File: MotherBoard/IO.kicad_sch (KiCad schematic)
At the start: 9 parts, among them J301 1376357-3, J302 Conn_01x04_Pin, J303 430450200

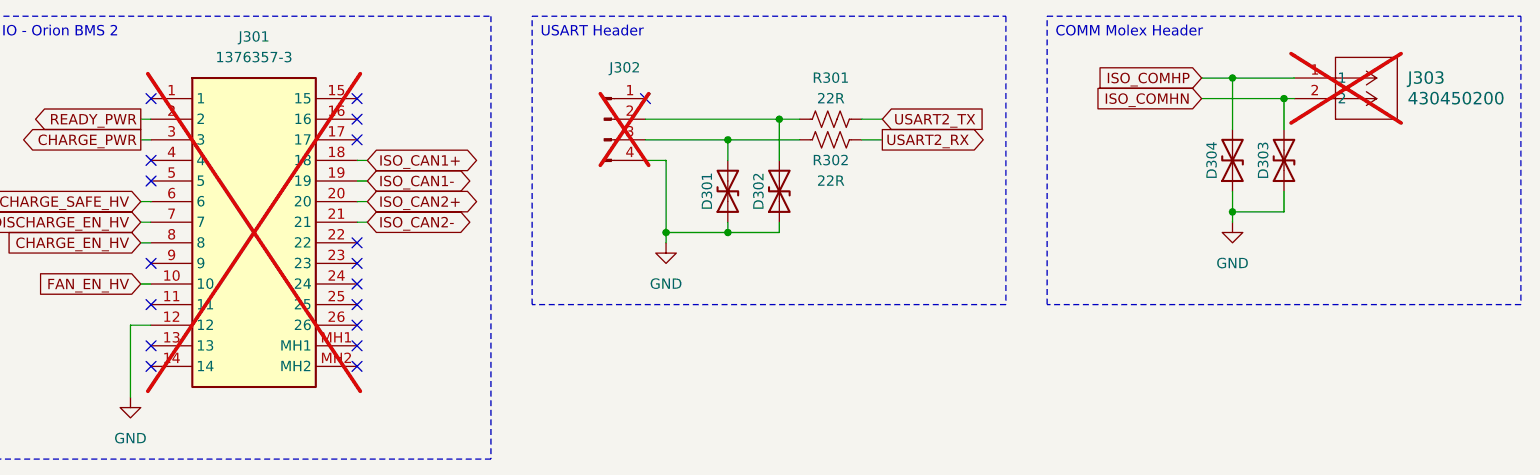
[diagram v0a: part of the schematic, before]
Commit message: BOM completed + All 3D models added + Initial board shape complete
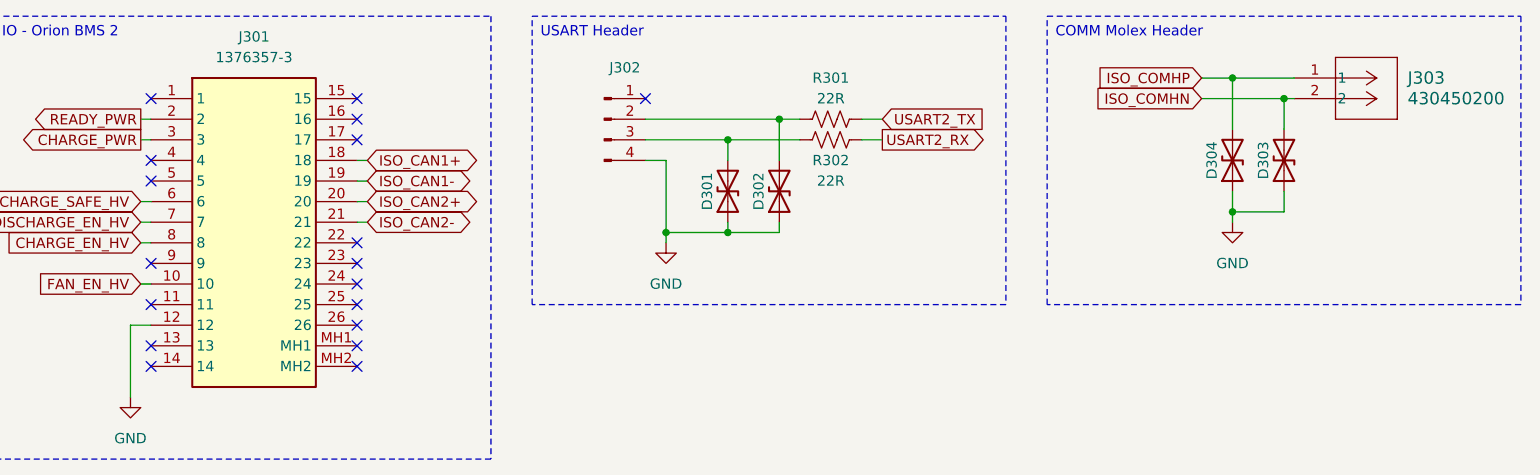
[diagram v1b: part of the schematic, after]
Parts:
- J301, J302, J303: now fitted
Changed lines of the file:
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@@
 		(in_bom yes)
 		(on_board yes)
-		(dnp yes)
+		(dnp no)
 		(property "Reference" "J302"
 			(at 106.68 31.75 0)
@@
 		(in_bom yes)
 		(on_board yes)
-		(dnp yes)
+		(dnp no)
 		(fields_autoplaced yes)
 		(property "Reference" "J301"
@@
 		(in_bom yes)
 		(on_board yes)
-		(dnp yes)
+		(dnp no)
 		(fields_autoplaced yes)
 		(property "Reference" "J303"

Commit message: Finished layout need to route
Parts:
- added D? (x2): D_TVS, Diode_SMD:D_SOD-323, symbol Device:D_TVS
- added J?: 430450200, molex_comm:CON_430450200_MOL, symbol molex_comm:430450200
- renumbered D304 to D303, D303 to D304
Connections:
- net GND: now also D?.1 (A1), D?.1 (A1)
- new net ISO_COMLN: D?.2 (A2), J?.2
- new net ISO_COMLP: D?.2 (A2), J?.1

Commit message: Finished motherboard. Need to review BOM
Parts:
- removed D304, D? (x2): D_TVS, Diode_SMD:D_SOD-323, symbol Device:D_TVS
- added C301: 1u, Capacitor_SMD:C_0402_1005Metric, symbol Device:C
- added D301, D305: D_TVS, Diode_SMD:D_SOD-323, symbol Device:D_TVS
- added F301, F302: Fuse, Fuse:Fuse_0805_2012Metric, symbol Device:Fuse
- added J301: Conn_01x04_Pin, Connector_PinHeader_2.54mm:PinHeader_1x04_P2.54mm_Vertical, symbol Connector:Conn_01x04_Pin
- added J306: Conn_01x02_Pin, Connector_PinHeader_2.54mm:PinHeader_1x02_P2.54mm_Vertical, symbol Connector:Conn_01x02_Pin
- added R301, R302: 22R, Resistor_SMD:R_1206_3216Metric, symbol Device:R_US
- added R305: 2.2k, Resistor_SMD:R_1206_3216Metric, symbol Device:R_US
- D303: Manufacturer_Part_Number (none) -> PESD3V3L1BA,115
- gave numbers to parts that had none: 1
- renumbered D301 to D302, D302 to D304, J301 to J303, J303 to J304, R301 to R303, R302 to R304
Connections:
- net GND: now also J302.1 (Pin_1), C301.2, D301.1 (A1), D305.1 (A1), J301.1 (Pin_1), J306.1 (Pin_1); no longer J302.4 (Pin_4)
- net ISO_COMHP: no longer D303.2 (A2)
- new net: D301.2 (A2), J301.3 (Pin_3), R302.1
- new net: D303.2 (A2), J301.2 (Pin_2), R301.1
- new net: F301.2, J301.4 (Pin_4)
- new net: D305.2 (A2), J306.2 (Pin_2), R305.1
- new net: F302.2, J302.4 (Pin_4)
- new net +5V: F301.1, F302.1
- new net ADC_IN: C301.1, R305.2
- new net UART4_RX: R302.2
- new net UART4_TX: R301.2
- no-connect marks 18 -> 17
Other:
- moved on the sheet: D302, D304, J302, J303, J304, J305, R303, R304

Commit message: Fixed power routing mistake + finished BOM + generated manufacturing files
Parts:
- D305: Manufacturer_Part_Number (none) -> PESD3V3L1BA,115
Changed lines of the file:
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@@
+			)
+		)
+		(property "JLC" ""
+			(at 59.69 167.64 0)
+			(effects
+				(font
+					(size 1.27 1.27)
+				)
+				(hide yes)
 			)
 		)
@@
 			)
 		)
+		(property "JLC" ""
+			(at 59.69 165.1 0)
+			(effects
+				(font
+					(size 1.27 1.27)
+				)
+				(hide yes)
+			)
+		)
 		(pin "2"
 		)
@@
 		)
 		(property "Sim.Type" ""
+			(at 31.75 165.1 0)
+			(effects
+				(font
+					(size 1.27 1.27)
+				)
+				(hide yes)
+			)
+		)
+		(property "JLC" ""
 			(at 31.75 165.1 0)
 			(effects
@@
 			)
 		)
+		(property "JLC" ""
+			(at 160.02 36.83 0)
+			(effects
+				(font
+					(size 1.27 1.27)
+				)
+				(hide yes)
+			)
+		)
 		(pin "1"
 		)
@@
 			)
 		)
+		(property "Manufacturer_Part_Number" "PESD3V3L1BA,115"
+			(at 175.26 41.91 0)
+			(effects
+				(font
+					(size 1.27 1.27)
+				)
+				(hide yes)
+			)
+		)
+		(property "JLC" ""
+			(at 175.26 41.91 0)
+			(effects
+				(font
+					(size 1.27 1.27)
+				)
+				(hide yes)
+			)
+		)
 		(pin "1"
 		)
@@
 		)
 		(property "Sim.Type" ""
+			(at 33.02 121.92 0)
+			(effects
+				(font
+					(size 1.27 1.27)
+				)
+				(hide yes)
+			)
+		)
+		(property "JLC" ""
 			(at 33.02 121.92 0)
 			(effects
@@
 			)
 		)
+		(property "JLC" ""
+			(at 60.96 124.46 0)
+			(effects
+				(font
+					(size 1.27 1.27)
+				)
+				(hide yes)
+			)
+		)
 		(pin "2"
 		)
@@
 			)
 		)
+		(property "JLC" ""
+			(at 53.34 173.99 0)
+			(effects
+				(font
+					(size 1.27 1.27)
+				)
+				(hide yes)
+			)
+		)
 		(pin "1"
 		)
@@
 		)
 		(property "Manufacturer_Part_Number" "PESD3V3L1BA,115"
+			(at 54.61 130.81 0)
+			(effects
+				(font
+					(size 1.27 1.27)
+				)
+				(hide yes)
+			)
+		)
+		(property "JLC" ""
 			(at 54.61 130.81 0)
 			(effects
@@
 			)
 		)
+		(property "JLC" ""
+			(at 43.18 160.02 0)
+			(effects
+				(font
+					(size 1.27 1.27)
+				)
+				(hide yes)
+			)
+		)
 		(pin "1"
 		)
@@
 		)
 		(property "Manufacturer_Part_Number" "FRC1206J220 TS"
+			(at 181.61 36.83 0)
+			(effects
+				(font
+					(size 1.27 1.27)
+				)
+				(hide yes)
+			)
+		)
+		(property "JLC" ""
 			(at 181.61 36.83 0)
 			(effects
@@
 			)
 		)
+		(property "JLC" ""
+			(at 46.99 43.18 0)
+			(effects
+				(font
+					(size 1.27 1.27)
+				)
+				(hide yes)
+			)
+		)
 		(pin "14"
 		)
@@
 			)
 		)
+		(property "JLC" ""
+			(at 123.19 33.02 0)
+			(effects
+				(font
+					(size 1.27 1.27)
+				)
+				(hide yes)
+			)
+		)
 		(pin "1"
 		)
@@
 		)
 		(property "Manufacturer_Part_Number" "PESD3V3L1BA,115"
+			(at 46.99 173.99 0)
+			(effects
+				(font
+					(size 1.27 1.27)
+				)
+				(hide yes)
+			)
+		)
+		(property "JLC" ""
 			(at 46.99 173.99 0)
 			(effects
@@
 			)
 		)
+		(property "JLC" ""
+			(at 44.45 115.57 0)
+			(effects
+				(font
+					(size 1.27 1.27)
+				)
+				(hide yes)
+			)
+		)
 		(pin "1"
 		)
@@
 			)
 		)
+		(property "JLC" ""
+			(at 123.19 81.28 0)
+			(effects
+				(font
+					(size 1.27 1.27)
+				)
+				(hide yes)
+			)
+		)
 		(pin "1"
 		)
@@
 			)
 		)
+		(property "JLC" ""
+			(at 190.5 41.91 0)
+			(effects
+				(font
+					(size 1.27 1.27)
+				)
+				(hide yes)
+			)
+		)
 		(pin "1"
 		)
@@
 			)
 		)
+		(property "JLC" ""
+			(at 48.26 130.81 0)
+			(effects
+				(font
+					(size 1.27 1.27)
+				)
+				(hide yes)
+			)
+		)
 		(pin "1"
 		)
@@
 			(at 60.96 121.92 0)
 			(effects
+				(font
+					(size 1.27 1.27)
+				)
+				(hide yes)
+			)
+		)
+		(property "JLC" ""
+			(at 60.96 121.92 0)
+			(effects

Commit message: Daughterboard 100% Complete + Edited Motherboard BOM
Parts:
- J301, J302, J303, J304, J305, J306: now not fitted
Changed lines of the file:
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@@
 		(in_bom yes)
 		(on_board yes)
-		(dnp no)
+		(dnp yes)
 		(property "Reference" "J301"
 			(at 34.29 158.75 0)
@@
 		(in_bom yes)
 		(on_board yes)
-		(dnp no)
+		(dnp yes)
 		(fields_autoplaced yes)
 		(property "Reference" "J306"
@@
 		(in_bom yes)
 		(on_board yes)
-		(dnp no)
+		(dnp yes)
 		(property "Reference" "J302"
 			(at 35.56 115.57 0)
@@
 		(in_bom yes)
 		(on_board yes)
-		(dnp no)
+		(dnp yes)
 		(fields_autoplaced yes)
 		(property "Reference" "J303"
@@
 		(in_bom yes)
 		(on_board yes)
-		(dnp no)
+		(dnp yes)
 		(fields_autoplaced yes)
 		(property "Reference" "J304"
@@
 		(in_bom yes)
 		(on_board yes)
-		(dnp no)
+		(dnp yes)
 		(fields_autoplaced yes)
 		(property "Reference" "J305"

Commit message: Both boards complete
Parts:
- C301: JLCPCB Part # (none) -> C29266
- D301, D302, D303, D304, D305: JLCPCB Part # (none) -> C51450
- F301, F302: JLCPCB Part # (none) -> C269104
- R301, R302, R303, R304: JLCPCB Part # (none) -> C2907457
- R305: JLCPCB Part # (none) -> C26038; Manufacturer_Part_Number FRC1206J220 TS -> 1206W4J0222T5E
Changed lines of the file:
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@@
 			)
 		)
-		(property "JLC" ""
+		(property "JLCPCB Part #" "C2907457"
 			(at 59.69 167.64 0)
 			(effects
@@
 			)
 		)
-		(property "JLC" ""
+		(property "JLCPCB Part #" "C2907457"
 			(at 59.69 165.1 0)
 			(effects
@@
 		)
 		(property "Sim.Type" ""
-			(at 31.75 165.1 0)
-			(effects
-				(font
-					(size 1.27 1.27)
-				)
-				(hide yes)
-			)
-		)
-		(property "JLC" ""
 			(at 31.75 165.1 0)
 			(effects
@@
 			)
 		)
-		(property "JLC" ""
-			(at 160.02 36.83 0)
-			(effects
-				(font
-					(size 1.27 1.27)
-				)
-				(hide yes)
-			)
-		)
 		(pin "1"
 		)
@@
 			)
 		)
-		(property "JLC" ""
+		(property "JLCPCB Part #" "C51450"
 			(at 175.26 41.91 0)
 			(effects
@@
 		)
 		(property "Sim.Type" ""
-			(at 33.02 121.92 0)
-			(effects
-				(font
-					(size 1.27 1.27)
-				)
-				(hide yes)
-			)
-		)
-		(property "JLC" ""
 			(at 33.02 121.92 0)
 			(effects
@@
 			)
 		)
-		(property "JLC" ""
+		(property "JLCPCB Part #" "C2907457"
 			(at 60.96 124.46 0)
 			(effects
@@
 			)
 		)
-		(property "JLC" ""
+		(property "JLCPCB Part #" "C51450"
 			(at 53.34 173.99 0)
 			(effects
@@
 			)
 		)
-		(property "JLC" ""
+		(property "JLCPCB Part #" "C51450"
 			(at 54.61 130.81 0)
 			(effects
@@
 			)
 		)
-		(property "JLC" ""
+		(property "JLCPCB Part #" "C269104"
 			(at 43.18 160.02 0)
 			(effects
@@
 			)
 		)
-		(property "Manufacturer_Part_Number" "FRC1206J220 TS"
+		(property "Manufacturer_Part_Number" "1206W4J0222T5E"
 			(at 181.61 36.83 0)
 			(effects
@@
 			)
 		)
-		(property "JLC" ""
+		(property "JLCPCB Part #" "C26038"
 			(at 181.61 36.83 0)
 			(effects
@@
 			)
 		)
-		(property "JLC" ""
-			(at 46.99 43.18 0)
-			(effects
-				(font
-					(size 1.27 1.27)
-				)
-				(hide yes)
-			)
-		)
 		(pin "14"
 		)
@@
 			)
 		)
-		(property "JLC" ""
-			(at 123.19 33.02 0)
-			(effects
-				(font
-					(size 1.27 1.27)
-				)
-				(hide yes)
-			)
-		)
 		(pin "1"
 		)
@@
 			)
 		)
-		(property "JLC" ""
+		(property "JLCPCB Part #" "C51450"
 			(at 46.99 173.99 0)
 			(effects
@@
 			)
 		)
-		(property "JLC" ""
+		(property "JLCPCB Part #" "C269104"
 			(at 44.45 115.57 0)
 			(effects
@@
 			)
 		)
-		(property "JLC" ""
-			(at 123.19 81.28 0)
-			(effects
-				(font
-					(size 1.27 1.27)
-				)
-				(hide yes)
-			)
-		)
 		(pin "1"
 		)
@@
 			)
 		)
-		(property "JLC" ""
+		(property "JLCPCB Part #" "C29266"
 			(at 190.5 41.91 0)
 			(effects
@@
 			)
 		)
-		(property "JLC" ""
+		(property "JLCPCB Part #" "C51450"
 			(at 48.26 130.81 0)
 			(effects
@@
 			)
 		)
-		(property "JLC" ""
+		(property "JLCPCB Part #" "C2907457"
 			(at 60.96 121.92 0)
 			(effects
